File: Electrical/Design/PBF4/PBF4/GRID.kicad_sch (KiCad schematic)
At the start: 9 parts, among them J10 TE Connectivity 84982-8, J11 TE Connectivity 84982-8, J4 TE Connectivity 84982-8, J5 TE Connectivity 84982-8, J6 TE Connectivity 84982-8, J7 TE Connectivity 84982-8, J8 TE Connectivity 84982-8, J9 TE Connectivity 84982-8, M1 (NF)

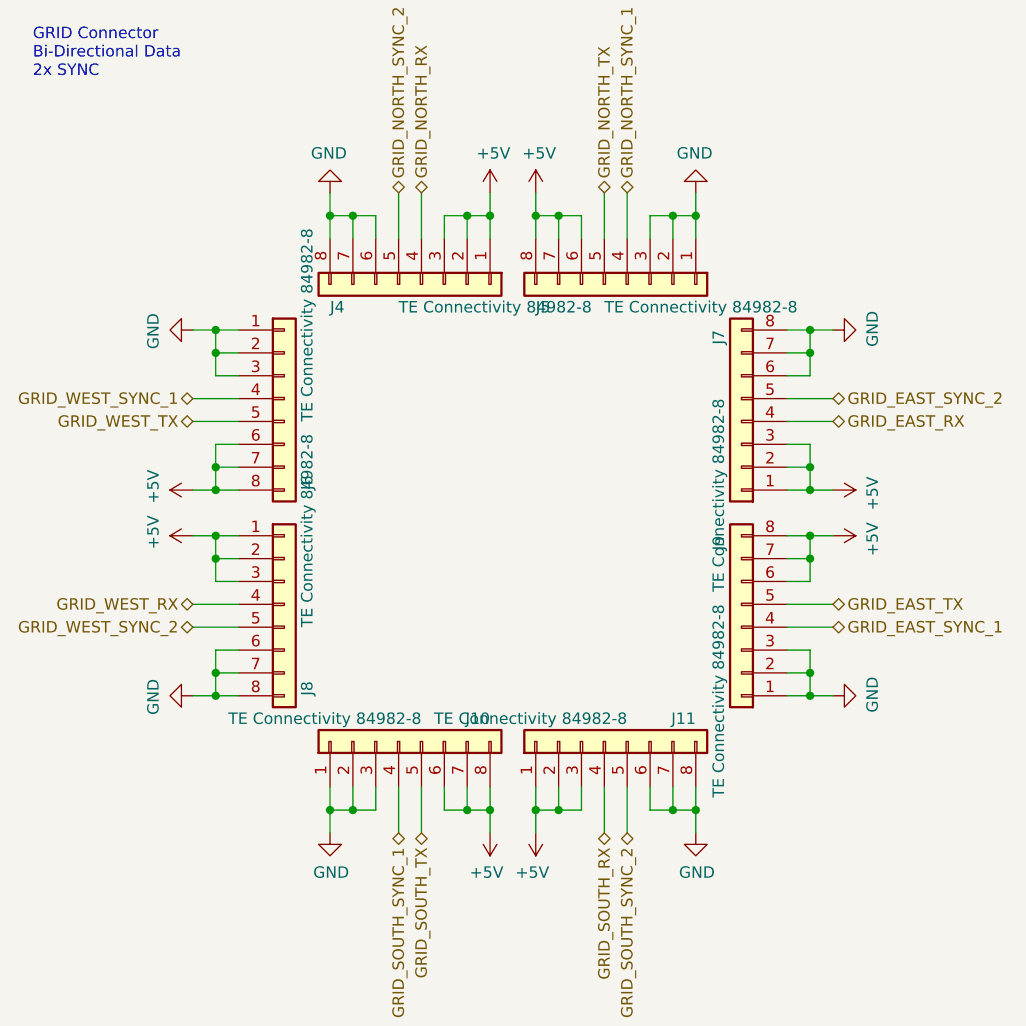
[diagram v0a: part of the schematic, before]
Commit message: SUKU port connector pinout fixed MAN-33
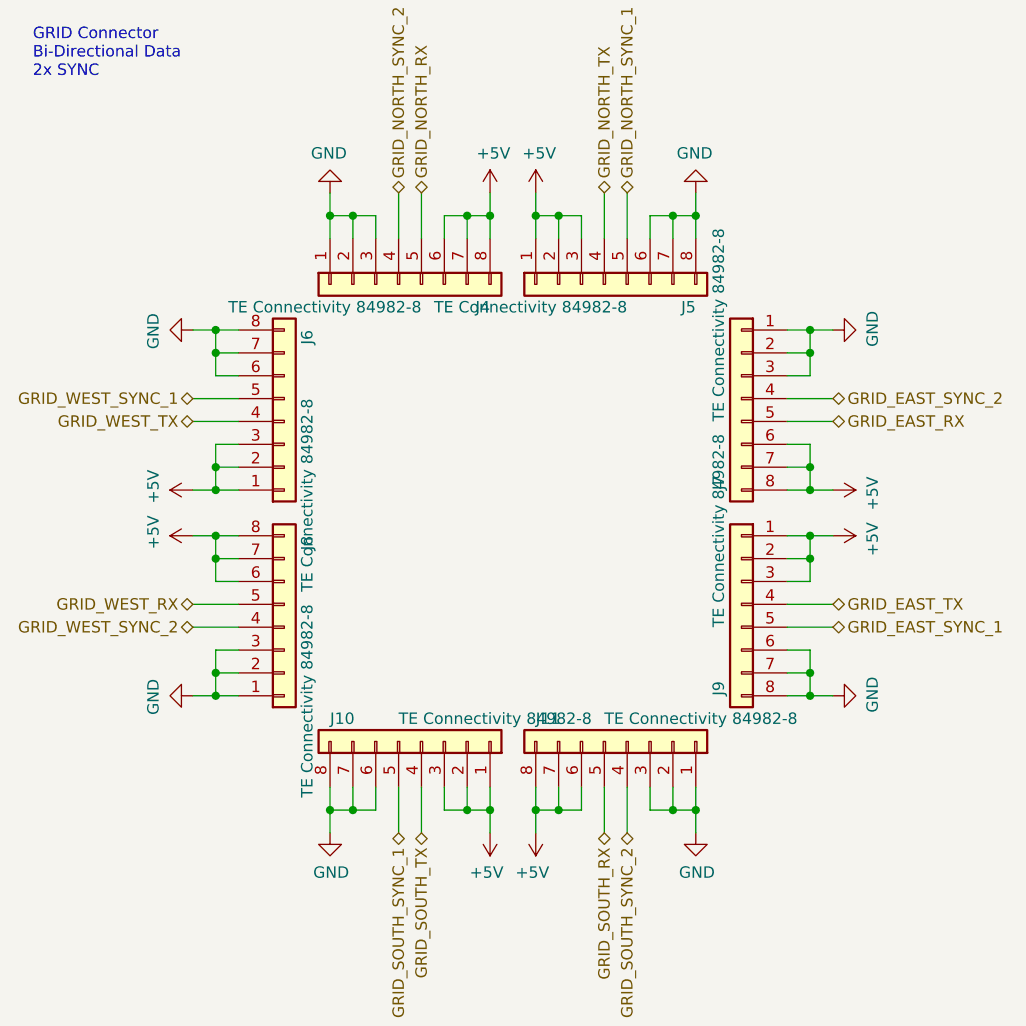
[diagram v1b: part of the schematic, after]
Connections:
- net +5V: now also J10.1 (Pin_1), J10.2 (Pin_2), J10.3 (Pin_3), J11.6 (Pin_6), J11.7 (Pin_7), J11.8 (Pin_8), J4.6 (Pin_6), J4.7 (Pin_7), J4.8 (Pin_8), J5.1 (Pin_1), J5.2 (Pin_2), J5.3 (Pin_3), J6.1 (Pin_1), J6.2 (Pin_2), J6.3 (Pin_3), J7.6 (Pin_6), J7.7 (Pin_7), J7.8 (Pin_8), J8.6 (Pin_6), J8.7 (Pin_7), J8.8 (Pin_8), J9.1 (Pin_1), J9.2 (Pin_2), J9.3 (Pin_3); no longer J10.6 (Pin_6), J10.7 (Pin_7), J10.8 (Pin_8), J11.1 (Pin_1), J11.2 (Pin_2), J11.3 (Pin_3), J4.1 (Pin_1), J4.2 (Pin_2), J4.3 (Pin_3), J5.6 (Pin_6), J5.7 (Pin_7), J5.8 (Pin_8), J6.6 (Pin_6), J6.7 (Pin_7), J6.8 (Pin_8), J7.1 (Pin_1), J7.2 (Pin_2), J7.3 (Pin_3), J8.1 (Pin_1), J8.2 (Pin_2), J8.3 (Pin_3), J9.6 (Pin_6), J9.7 (Pin_7), J9.8 (Pin_8)
- net GND: now also J10.6 (Pin_6), J10.7 (Pin_7), J10.8 (Pin_8), J11.1 (Pin_1), J11.2 (Pin_2), J11.3 (Pin_3), J4.1 (Pin_1), J4.2 (Pin_2), J4.3 (Pin_3), J5.6 (Pin_6), J5.7 (Pin_7), J5.8 (Pin_8), J6.6 (Pin_6), J6.7 (Pin_7), J6.8 (Pin_8), J7.1 (Pin_1), J7.2 (Pin_2), J7.3 (Pin_3), J8.1 (Pin_1), J8.2 (Pin_2), J8.3 (Pin_3), J9.6 (Pin_6), J9.7 (Pin_7), J9.8 (Pin_8); no longer J10.1 (Pin_1), J10.2 (Pin_2), J10.3 (Pin_3), J11.6 (Pin_6), J11.7 (Pin_7), J11.8 (Pin_8), J4.6 (Pin_6), J4.7 (Pin_7), J4.8 (Pin_8), J5.1 (Pin_1), J5.2 (Pin_2), J5.3 (Pin_3), J6.1 (Pin_1), J6.2 (Pin_2), J6.3 (Pin_3), J7.6 (Pin_6), J7.7 (Pin_7), J7.8 (Pin_8), J8.6 (Pin_6), J8.7 (Pin_7), J8.8 (Pin_8), J9.1 (Pin_1), J9.2 (Pin_2), J9.3 (Pin_3)
- net GRID_EAST_RX: now also J7.5 (Pin_5); no longer J7.4 (Pin_4)
- net GRID_EAST_SYNC_1: now also J9.5 (Pin_5); no longer J9.4 (Pin_4)
- net GRID_EAST_SYNC_2: now also J7.4 (Pin_4); no longer J7.5 (Pin_5)
- net GRID_EAST_TX: now also J9.4 (Pin_4); no longer J9.5 (Pin_5)
- net GRID_NORTH_RX: now also J4.5 (Pin_5); no longer J4.4 (Pin_4)
- net GRID_NORTH_SYNC_1: now also J5.5 (Pin_5); no longer J5.4 (Pin_4)
- net GRID_NORTH_SYNC_2: now also J4.4 (Pin_4); no longer J4.5 (Pin_5)
- net GRID_NORTH_TX: now also J5.4 (Pin_4); no longer J5.5 (Pin_5)
- net GRID_SOUTH_RX: now also J11.5 (Pin_5); no longer J11.4 (Pin_4)
- net GRID_SOUTH_SYNC_1: now also J10.5 (Pin_5); no longer J10.4 (Pin_4)
- net GRID_SOUTH_SYNC_2: now also J11.4 (Pin_4); no longer J11.5 (Pin_5)
- net GRID_SOUTH_TX: now also J10.4 (Pin_4); no longer J10.5 (Pin_5)
- net GRID_WEST_RX: now also J8.5 (Pin_5); no longer J8.4 (Pin_4)
- net GRID_WEST_SYNC_1: now also J6.5 (Pin_5); no longer J6.4 (Pin_4)
- net GRID_WEST_SYNC_2: now also J8.4 (Pin_4); no longer J8.5 (Pin_5)
- net GRID_WEST_TX: now also J6.4 (Pin_4); no longer J6.5 (Pin_5)
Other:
- moved on the sheet: J10, J11, J4, J5, J7, J9

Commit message: SUKU rf matching done
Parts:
- J501: renamed from J6; value TE Connectivity 84982-8 -> AFB10-S08LCA-00
- J502: renamed from J8; value TE Connectivity 84982-8 -> AFB10-S08LCA-00
- J503: renamed from J4; value TE Connectivity 84982-8 -> AFB10-S08LCA-00
- J504: renamed from J10; value TE Connectivity 84982-8 -> AFB10-S08LCA-00
- J505: renamed from J5; value TE Connectivity 84982-8 -> AFB10-S08LCA-00
- J506: renamed from J11; value TE Connectivity 84982-8 -> AFB10-S08LCA-00
- J507: renamed from J7; value TE Connectivity 84982-8 -> AFB10-S08LCA-00
- J508: renamed from J9; value TE Connectivity 84982-8 -> AFB10-S08LCA-00
- renumbered M1 to M501
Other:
- note added: "500"
- note added: "Connector: AFB10-S08LCA-00 or TE Connectivity 84982-8"
- moved on the sheet: J501, J502, J503, J504, J505, J506, J507, J508

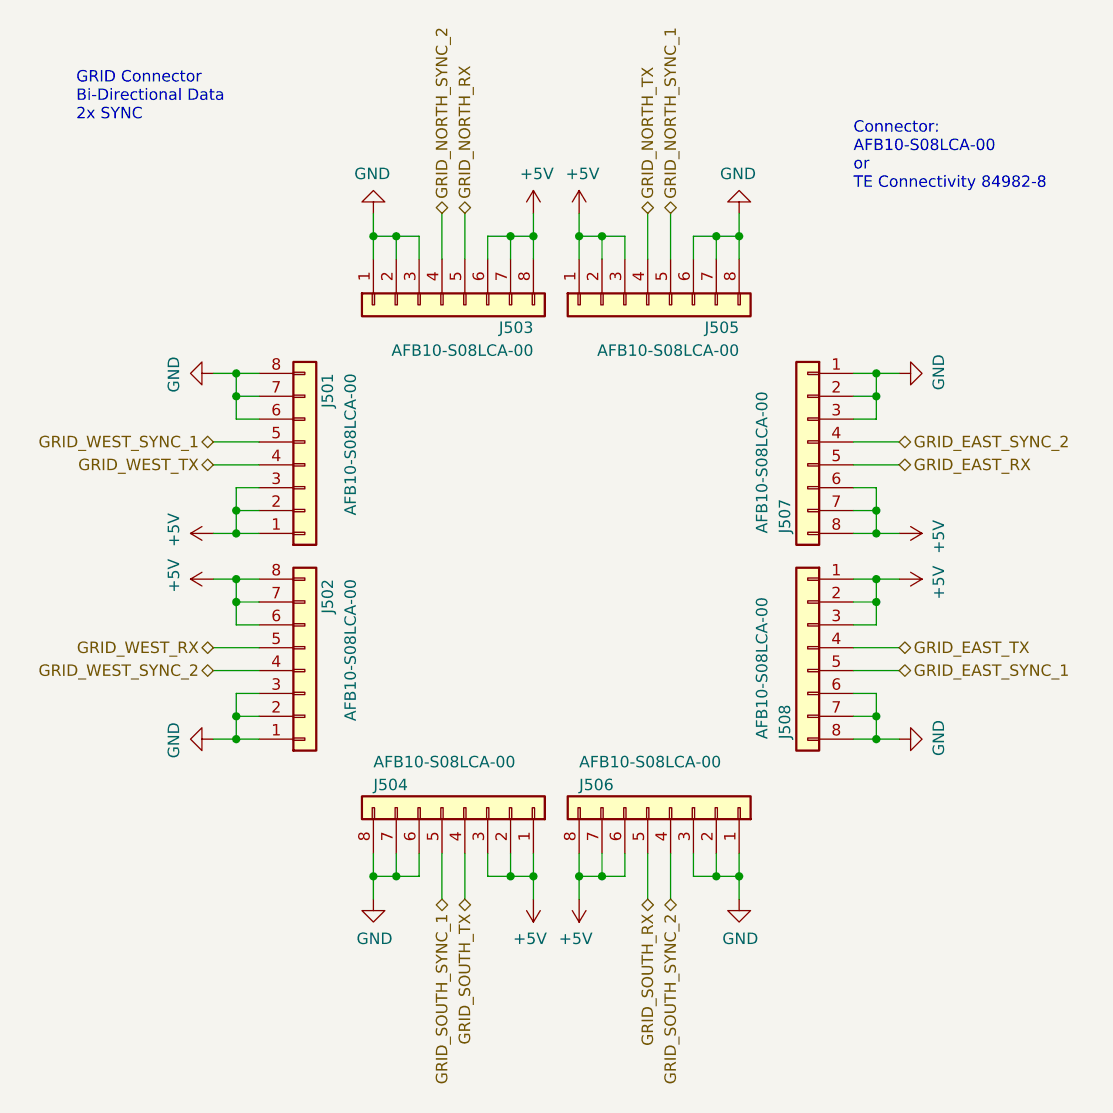
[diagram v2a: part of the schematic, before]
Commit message: SUKU PBF4 pcb updated to use battery conn
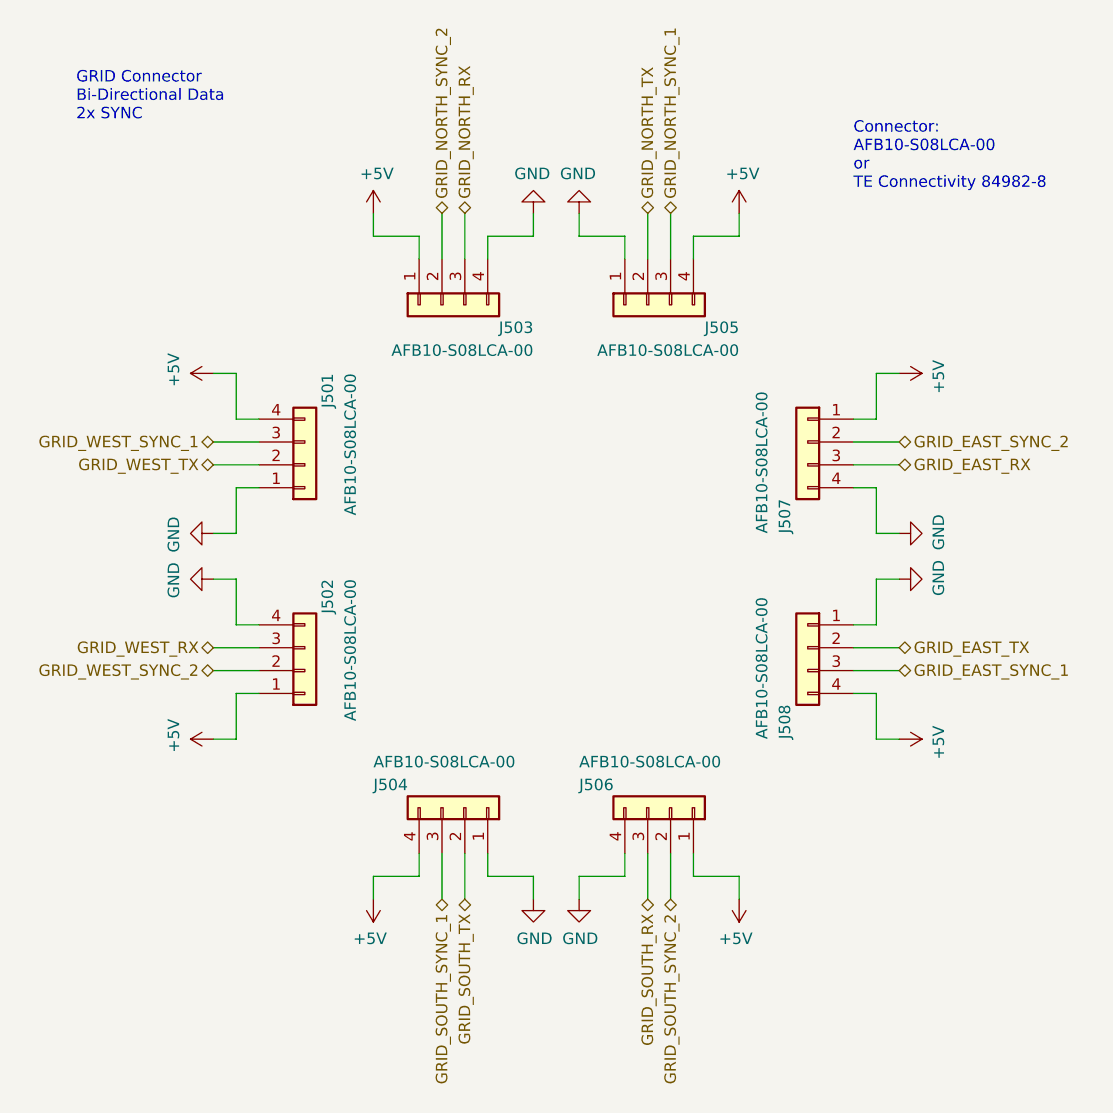
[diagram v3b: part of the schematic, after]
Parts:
- J501, J502, J503, J504, J505, J506, J507, J508: footprint suku_basics:grid_ffc_8_vertical_smd -> suku_basics:J_INTERFACE_SPRINGPATTERN; symbol Connector_Generic:Conn_01x08 -> Connector_Generic:Conn_01x04; now left out of the parts list
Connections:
- net +5V: now also J501.4 (Pin_4), J502.1 (Pin_1), J503.1 (Pin_1), J504.4 (Pin_4), J505.4 (Pin_4), J506.1 (Pin_1), J507.1 (Pin_1), J508.4 (Pin_4); no longer J501.1 (Pin_1), J501.2 (Pin_2), J501.3 (Pin_3), J502.6 (Pin_6), J502.7 (Pin_7), J502.8 (Pin_8), J503.6 (Pin_6), J503.7 (Pin_7), J503.8 (Pin_8), J504.1 (Pin_1), J504.2 (Pin_2), J504.3 (Pin_3), J505.1 (Pin_1), J505.2 (Pin_2), J505.3 (Pin_3), J506.6 (Pin_6), J506.7 (Pin_7), J506.8 (Pin_8), J507.6 (Pin_6), J507.7 (Pin_7), J507.8 (Pin_8), J508.1 (Pin_1), J508.2 (Pin_2), J508.3 (Pin_3)
- net GND: now also J501.1 (Pin_1), J502.4 (Pin_4), J503.4 (Pin_4), J504.1 (Pin_1), J505.1 (Pin_1), J506.4 (Pin_4), J507.4 (Pin_4), J508.1 (Pin_1); no longer J501.6 (Pin_6), J501.7 (Pin_7), J501.8 (Pin_8), J502.1 (Pin_1), J502.2 (Pin_2), J502.3 (Pin_3), J503.1 (Pin_1), J503.2 (Pin_2), J503.3 (Pin_3), J504.6 (Pin_6), J504.7 (Pin_7), J504.8 (Pin_8), J505.6 (Pin_6), J505.7 (Pin_7), J505.8 (Pin_8), J506.1 (Pin_1), J506.2 (Pin_2), J506.3 (Pin_3), J507.1 (Pin_1), J507.2 (Pin_2), J507.3 (Pin_3), J508.6 (Pin_6), J508.7 (Pin_7), J508.8 (Pin_8)
- net GRID_EAST_RX: now also J507.3 (Pin_3); no longer J507.5 (Pin_5)
- net GRID_EAST_SYNC_1: now also J508.3 (Pin_3); no longer J508.5 (Pin_5)
- net GRID_EAST_SYNC_2: now also J507.2 (Pin_2); no longer J507.4 (Pin_4)
- net GRID_EAST_TX: now also J508.2 (Pin_2); no longer J508.4 (Pin_4)
- net GRID_NORTH_RX: now also J503.3 (Pin_3); no longer J503.5 (Pin_5)
- net GRID_NORTH_SYNC_1: now also J505.3 (Pin_3); no longer J505.5 (Pin_5)
- net GRID_NORTH_SYNC_2: now also J503.2 (Pin_2); no longer J503.4 (Pin_4)
- net GRID_NORTH_TX: now also J505.2 (Pin_2); no longer J505.4 (Pin_4)
- net GRID_SOUTH_RX: now also J506.3 (Pin_3); no longer J506.5 (Pin_5)
- net GRID_SOUTH_SYNC_1: now also J504.3 (Pin_3); no longer J504.5 (Pin_5)
- net GRID_SOUTH_SYNC_2: now also J506.2 (Pin_2); no longer J506.4 (Pin_4)
- net GRID_SOUTH_TX: now also J504.2 (Pin_2); no longer J504.4 (Pin_4)
- net GRID_WEST_RX: now also J502.3 (Pin_3); no longer J502.5 (Pin_5)
- net GRID_WEST_SYNC_1: now also J501.3 (Pin_3); no longer J501.5 (Pin_5)
- net GRID_WEST_SYNC_2: now also J502.2 (Pin_2); no longer J502.4 (Pin_4)
- net GRID_WEST_TX: now also J501.2 (Pin_2); no longer J501.4 (Pin_4)
